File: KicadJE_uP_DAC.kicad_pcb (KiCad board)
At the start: 2 copper layers, 100 x 100 mm, 216 parts, among them J201 CV1, J202 CV2, J203 OUT1, J204 OUT2, J205 IN1, J206 IN2, J301 AVR-ISP-6, J302 UART, J401 CV1, J402 CV2, J403 OUT1, J404 OUT2, J405 OUT3, J406 OUT4, J407 IN1, J408 IN2, J409 I2C, J501 BOOT, J502 UART, J503 USB_B_Micro, P201 Doepfer_Power_16pin, P401 Doepfer_Power_16pin, SW201 SW_SPDT, SW401 SW_SPDT, U201 TL072, U202 MCP4822, U301 ATmega32A-AU, U401 TL072, U402 TL072, U405 MCP4822, U501 AMS1117-3.3, U502 STM32F103C8Tx, Y301 16MHz, Y501 8 MHz

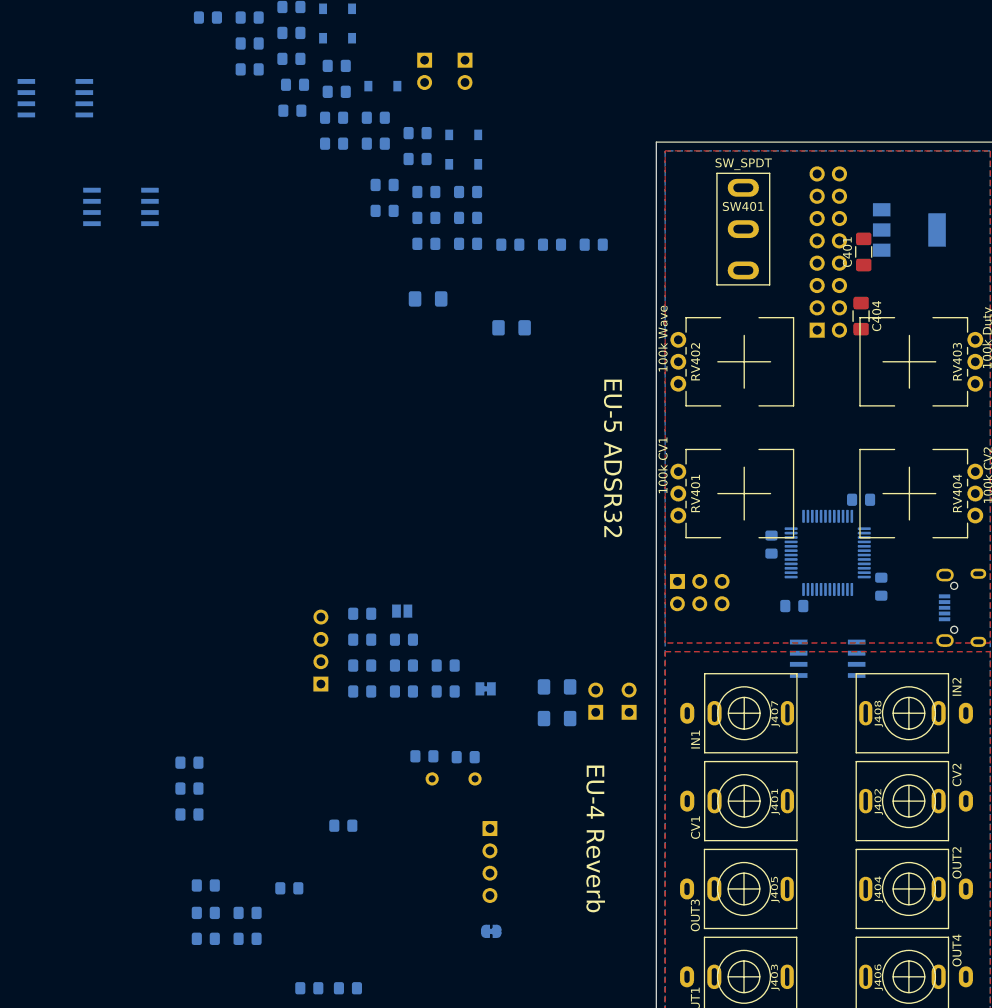
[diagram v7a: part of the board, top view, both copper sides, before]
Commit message: Power routed
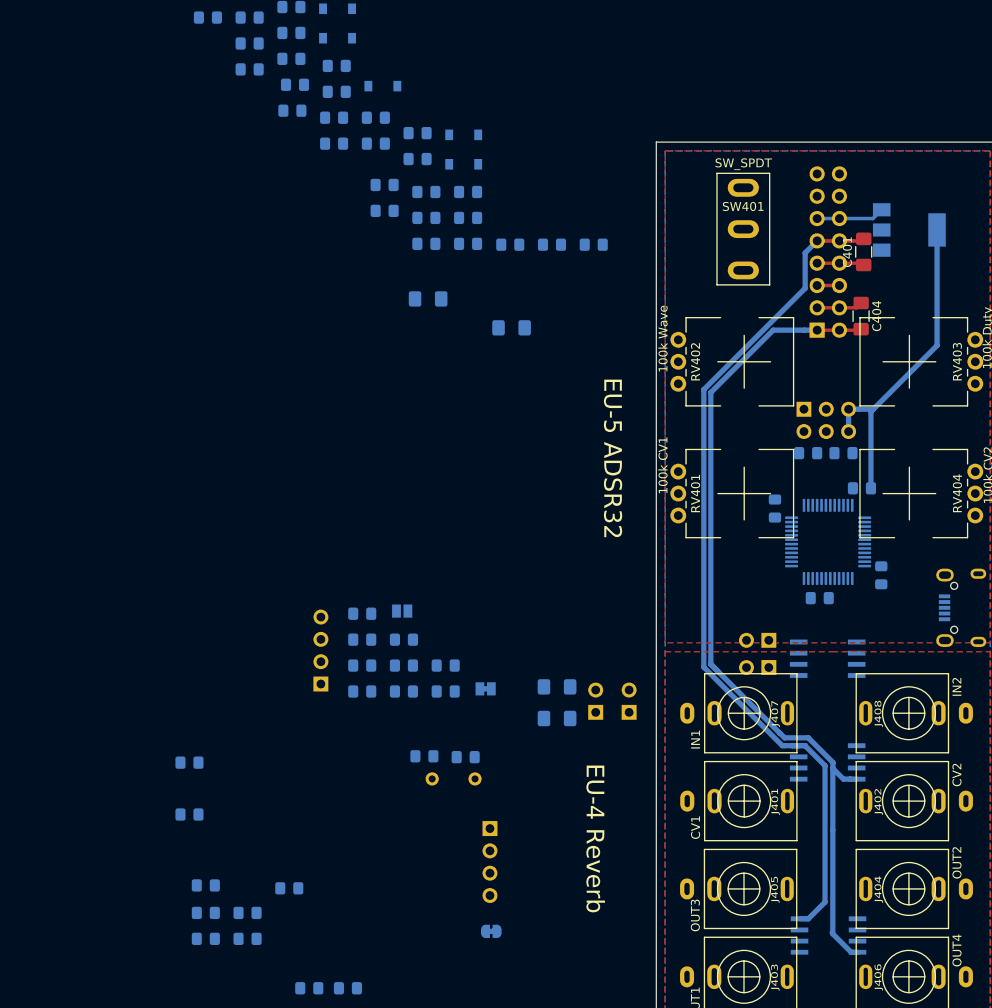
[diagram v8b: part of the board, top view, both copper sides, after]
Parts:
- moved U402 115.9 mm to (69.5, 120.6), turned to 180 degrees
- moved U401 115.6 mm to (69.6, 140.3), turned to 180 degrees
- moved R503 83.7 mm to (71.3, 85.4), turned to 0 degrees
- moved JP403 79.5 mm to (62.8, 109.8), turned to 90 degrees
- moved JP404 74.5 mm to (62.8, 106.7), turned to 90 degrees
- moved R506 67.8 mm to (67.3, 85.4)
- moved J501 24.3 mm to (66.8, 80.4)
- moved C504 11.4 mm to (73.4, 89.4), turned to 0 degrees
- moved C505 10.5 mm to (75.6, 99.3), turned to 270 degrees
- moved C503 9.85 mm to (63.5, 91.7), turned to 90 degrees
- moved C506 8.21 mm to (68.6, 101.9), turned to 180 degrees
- moved U502 1.25 mm to (69.5, 95.5), turned to 90 degrees
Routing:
- net -12V: track 73.7 -> 181.1 mm
- net +12V: track 87.1 -> 184.8 mm
- net +3V3: track 0.00 -> 37.9 mm
- net GND: track 49.0 -> 62.2 mm
- net +5V: track 201.2 -> 209.0 mm
